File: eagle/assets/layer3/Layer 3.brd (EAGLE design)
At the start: 196 x 158 mm, 84 parts, among them Q2 AO3402, X1 SM06B-SRSS-TB, Y1 8MHz

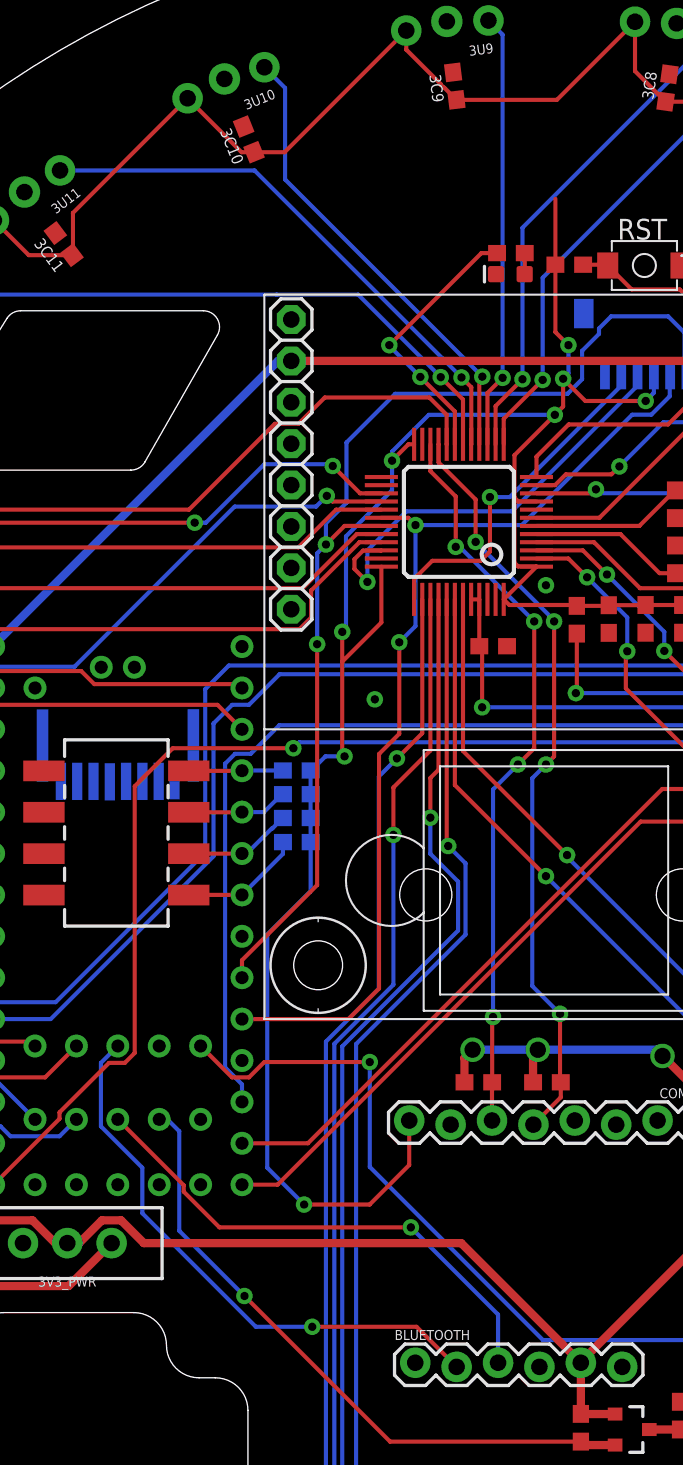
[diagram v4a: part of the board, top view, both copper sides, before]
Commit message: Edited teensy 4 pin out
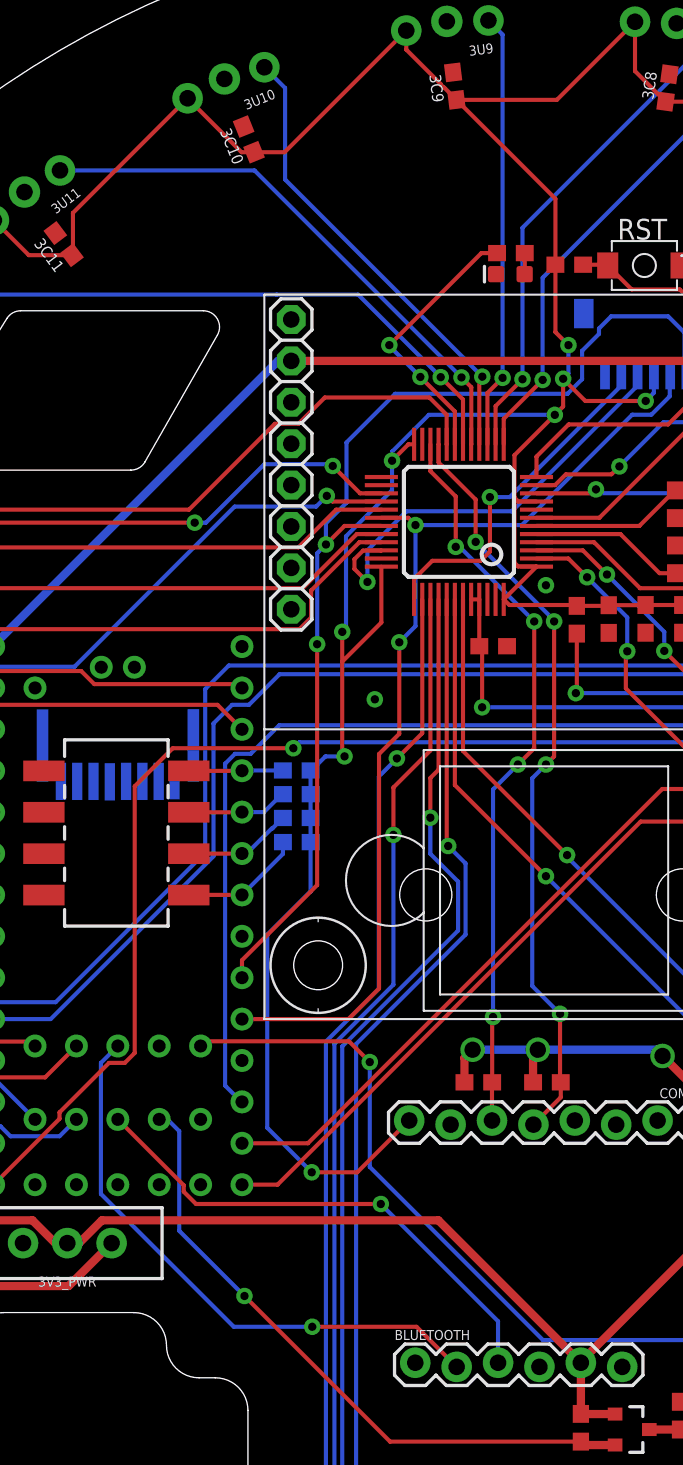
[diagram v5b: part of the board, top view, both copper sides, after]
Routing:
- net 3V3_SWITCH: track 577.5 -> 581.4 mm
- net RX_BT: track 34.9 -> 35.7 mm
- net ESC_LV: track 47.4 -> 46.9 mm
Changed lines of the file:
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@@
 </layers>
 <board>
-<fusionsync huburn="a.YnVzaW5lc3M6Z21haWwxNDMxNzc3" projecturn="a.YnVzaW5lc3M6Z21haWwxNDMxNzc3IzIwMjIwMTE1NDg1NTYyMzgx" f3durn="urn:adsk.wipprod:dm.lineage:7ikLfJsPR9eTqnN77vvEIg" pcbguid="" lastpulledtime="" lastsyncedchangeguid="" latestrevisionid="1eb35726-afcb-4420-9c79-5270dc816efc" lastsyncedrevisionid="1eb35726-afcb-4420-9c79-5270dc816efc" lastboardhashguid="961d5901-0f89-b416-3a91-9d1b3ab43cf4" lastpushedtime="2022-03-01T01:10:26Z" linktopcb3d="true"/>
+<fusionsync huburn="a.YnVzaW5lc3M6Z21haWwxNDMxNzc3" projecturn="a.YnVzaW5lc3M6Z21haWwxNDMxNzc3IzIwMjIwMTE1NDg1NTYyMzgx" f3durn="urn:adsk.wipprod:dm.lineage:7ikLfJsPR9eTqnN77vvEIg" pcbguid="" lastpulledtime="" lastsyncedchangeguid="" latestrevisionid="d040567a-c9aa-45d0-a0c7-126f738ef4e2" lastsyncedrevisionid="d040567a-c9aa-45d0-a0c7-126f738ef4e2" lastboardhashguid="c860b672-bc3c-8241-e7e5-cbe0f4989fd4" lastpushedtime="2022-03-01T08:50:26Z" linktopcb3d="true"/>
 <plain>
 <text x="-40.27" y="8.13" size="0.8128" layer="25" rot="R90">3.3V</text>
@@
 <wire x1="-35.8385875" y1="-19.9676125" x2="-42.802975" y2="-13.003225" width="0.508" layer="1"/>
 <wire x1="-32.0076" y1="-19.9676125" x2="-35.8385875" y2="-19.9676125" width="0.508" layer="1"/>
-<wire x1="-27.7453125" y1="-19.9676125" x2="-26.572" y2="-19.9676125" width="0.508" layer="1"/>
 <wire x1="-29.869209375" y1="-21.366409375" x2="-29.144109375" y2="-21.366409375" width="0.508" layer="1"/>
 <wire x1="-29.144109375" y1="-21.366409375" x2="-27.7453125" y2="-19.9676125" width="0.508" layer="1"/>
-<wire x1="-26.572" y1="-19.9676125" x2="-25.173203125" y2="-21.366409375" width="0.508" layer="1"/>
-<wire x1="-25.173203125" y1="-21.366409375" x2="-5.699090625" y2="-21.366409375" width="0.508" layer="1"/>
-<wire x1="-5.699090625" y1="-21.366409375" x2="1.64" y2="-28.7055" width="0.508" layer="1"/>
+<wire x1="-27.7453125" y1="-19.9676125" x2="-7.0978875" y2="-19.9676125" width="0.508" layer="1"/>
+<wire x1="-7.0978875" y1="-19.9676125" x2="1.64" y2="-28.7055" width="0.508" layer="1"/>
 <wire x1="3.743284375" y1="-31.8543625" x2="1.65240625" y2="-31.8543625" width="0.508" layer="1"/>
 <wire x1="1.65240625" y1="-31.8543625" x2="1.64371875" y2="-31.845675" width="0.508" layer="1"/>
@@
 <wire x1="45.571084375" y1="18.4119125" x2="45.571084375" y2="19.178815625" width="0.254" layer="1"/>
 <wire x1="45.571084375" y1="19.178815625" x2="48.880921875" y2="22.488653125" width="0.254" layer="1"/>
-<wire x1="0.079921875" y1="42.71384375" x2="0.079921875" y2="38.667053125" width="0.254" layer="1"/>
+<wire x1="0.079921875" y1="38.667053125" x2="0.079921875" y2="42.71384375" width="0.254" layer="1"/>
 <wire x1="-29.52406875" y1="41.84550625" x2="-29.52406875" y2="39.308071875" width="0.254" layer="1"/>
 <wire x1="-29.57920625" y1="39.252934375" x2="-29.52406875" y2="39.308071875" width="0.254" layer="1"/>
@@
 <wire x1="-1.097" y1="20.155" x2="-1.082" y2="20.14" width="0.254" layer="1"/>
 <wire x1="-2.43" y1="24.37548125" x2="-2.43" y2="20.37548125" width="0.254" layer="1"/>
-<wire x1="-15.34" y1="-19" x2="-11.3155" y2="-19" width="0.254" layer="1"/>
-<via x="-15.34" y="-19" extent="1-16" drill="0.508"/>
+<wire x1="-14.8705" y1="-17.0195" x2="-12.077" y2="-17.0195" width="0.254" layer="1"/>
+<via x="-14.8705" y="-17.0195" extent="1-16" drill="0.508"/>
 <wire x1="-17.6022" y1="-2.4444125" x2="-14.938325" y2="0.2194625" width="0.254" layer="16"/>
-<wire x1="-15.34" y1="-19" x2="-17.6022" y2="-16.7378" width="0.254" layer="16"/>
-<wire x1="-17.6022" y1="-16.7378" x2="-17.6022" y2="-2.4444125" width="0.254" layer="16"/>
+<wire x1="-14.8705" y1="-17.0195" x2="-17.6022" y2="-14.2878" width="0.254" layer="16"/>
+<wire x1="-17.6022" y1="-14.2878" x2="-17.6022" y2="-2.4444125" width="0.254" layer="16"/>
 <wire x1="-45.571084375" y1="-18.4119125" x2="-39.982996875" y2="-24" width="0.508" layer="1"/>
 <wire x1="-29.785" y1="-24" x2="-27.151409375" y2="-21.366409375" width="0.508" layer="1"/>
 <wire x1="-39.982996875" y1="-24" x2="-29.785" y2="-24" width="0.508" layer="1"/>
-<wire x1="-8.89" y1="-16.5745" x2="-8.89" y2="-13.843" width="0.254" layer="1"/>
-<wire x1="-11.3155" y1="-19" x2="-8.89" y2="-16.5745" width="0.254" layer="1"/>
-<wire x1="0.079921875" y1="42.71384375" x2="-5.989875" y2="48.783640625" width="0" layer="19" extent="1-1"/>
+<wire x1="-8.89" y1="-13.843" x2="-8.9005" y2="-13.843" width="0.254" layer="1"/>
+<wire x1="-8.9005" y1="-13.843" x2="-12.077" y2="-17.0195" width="0.254" layer="1"/>
+<wire x1="0.079921875" y1="42.71384375" x2="-5.989875" y2="48.783640625" width="0.254" layer="1"/>
 </signal>
 <signal name="5V_SWITCH">
@@
 <contactref element="TEENSY4" pad="D33"/>
 <via x="-11.31" y="-10.25683125" extent="1-16" drill="0.508"/>
-<wire x1="-17.78056875" y1="-10.25683125" x2="-11.31" y2="-10.25683125" width="0.254" layer="1"/>
-<wire x1="-18.7205375" y1="-11.1968" x2="-17.78056875" y2="-10.25683125" width="0.254" layer="1"/>
-<wire x1="-21.69" y1="-9.271" x2="-19.7642" y2="-11.1968" width="0.254" layer="1"/>
-<wire x1="-19.7642" y1="-11.1968" x2="-18.7205375" y2="-11.1968" width="0.254" layer="1"/>
+<wire x1="-12.586" y1="-8.98083125" x2="-21.39983125" y2="-8.98083125" width="0.254" layer="1"/>
+<wire x1="-21.69" y1="-9.271" x2="-21.39983125" y2="-8.98083125" width="0.254" layer="1"/>
+<wire x1="-12.586" y1="-8.98083125" x2="-11.31" y2="-10.25683125" width="0.254" layer="1"/>
 <wire x1="-11.31" y1="-10.25683125" x2="-11.31" y2="-16.69" width="0.254" layer="16"/>
 <wire x1="11.544853125" y1="-28.239759375" x2="13.310325" y2="-28.239759375" width="0.254" layer="16"/>
@@
 <wire x1="9.5198875" y1="10.4110875" x2="-16.8610875" y2="10.4110875" width="0.254" layer="16"/>
 <contactref element="TEENSY4" pad="D10"/>
-<wire x1="-19.15" y1="-12.7" x2="-19.15" y2="-11.6262625" width="0.254" layer="16"/>
-<wire x1="-19.15" y1="-11.6262625" x2="-20.1868" y2="-10.5894625" width="0.254" layer="16"/>
+<wire x1="-19.15" y1="-12.7" x2="-19.1867625" y2="-12.7" width="0.254" layer="16"/>
+<wire x1="-19.1867625" y1="-12.7" x2="-20.1868" y2="-11.6999625" width="0.254" layer="16"/>
 <wire x1="-20.1868" y1="8.0494625" x2="-19.5794625" y2="8.6568" width="0.254" layer="16"/>
 <wire x1="-18.615375" y1="8.6568" x2="-16.8610875" y2="10.4110875" width="0.254" layer="16"/>
 <wire x1="-19.5794625" y1="8.6568" x2="-18.615375" y2="8.6568" width="0.254" layer="16"/>
-<wire x1="-20.1868" y1="-10.5894625" x2="-20.1868" y2="8.0494625" width="0.254" layer="16"/>
+<wire x1="-20.1868" y1="-11.6999625" x2="-20.1868" y2="8.0494625" width="0.254" layer="16"/>
 </signal>
 <signal name="SDA0_TEE">
@@
 <contactref element="TEENSY4" pad="D29"/>
 <wire x1="-27.8068" y1="-10.3078" x2="-26.77" y2="-9.271" width="0.254" layer="16"/>
-<wire x1="-27.8068" y1="-10.3078" x2="-27.8068" y2="-14.2024625" width="0.254" layer="16"/>
-<wire x1="-25.2668" y1="-16.7424625" x2="-27.8068" y2="-14.2024625" width="0.254" layer="16"/>
-<wire x1="-25.2668" y1="-16.7424625" x2="-25.2668" y2="-19.53294375" width="0.254" layer="16"/>
-<wire x1="-18.29974375" y1="-26.5" x2="-14.84" y2="-26.5" width="0.254" layer="16"/>
+<wire x1="-27.8068" y1="-10.3078" x2="-27.8068" y2="-18.34844375" width="0.254" layer="16"/>
+<wire x1="-19.65524375" y1="-26.5" x2="-14.84" y2="-26.5" width="0.254" layer="16"/>
 <via x="-14.84" y="-26.5" extent="1-16" drill="0.508"/>
 <wire x1="-14.84" y1="-26.5" x2="-8.4395" y2="-26.5" width="0.254" layer="1"/>
 <wire x1="-8.4395" y1="-26.5" x2="-5.98" y2="-28.9595" width="0.254" layer="1"/>
-<wire x1="-25.2668" y1="-19.53294375" x2="-18.29974375" y2="-26.5" width="0.254" layer="16"/>
+<wire x1="-27.8068" y1="-18.34844375" x2="-19.65524375" y2="-26.5" width="0.254" layer="16"/>
 </signal>
 <signal name="TX_BT">
@@
 <wire x1="-26.77" y1="-13.773" x2="-22.7268" y2="-17.8162" width="0.254" layer="1"/>
 <wire x1="-22.7268" y1="-17.8162" x2="-22.7268" y2="-18.2094625" width="0.254" layer="1"/>
-<wire x1="-20.53685625" y1="-20.39940625" x2="-8.7885375" y2="-20.39940625" width="0.254" layer="1"/>
-<via x="-8.7885375" y="-20.39940625" extent="1-16" drill="0.508"/>
-<wire x1="-8.7885375" y1="-20.39940625" x2="-3.44" y2="-25.74794375" width="0.254" layer="16"/>
-<wire x1="-3.44" y1="-25.74794375" x2="-3.44" y2="-28.7055" width="0.254" layer="16"/>
-<wire x1="-22.7268" y1="-18.2094625" x2="-20.53685625" y2="-20.39940625" width="0.254" layer="1"/>
+<wire x1="-21.96985625" y1="-18.96640625" x2="-10.6340375" y2="-18.96640625" width="0.254" layer="1"/>
+<via x="-10.6340375" y="-18.96640625" extent="1-16" drill="0.508"/>
+<wire x1="-10.6340375" y1="-18.96640625" x2="-3.44" y2="-26.16044375" width="0.254" layer="16"/>
+<wire x1="-3.44" y1="-26.16044375" x2="-3.44" y2="-28.7055" width="0.254" layer="16"/>
+<wire x1="-22.7268" y1="-18.2094625" x2="-21.96985625" y2="-18.96640625" width="0.254" layer="1"/>
 </signal>
 <signal name="SERVO_HV">

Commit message: Edited cura
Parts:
- removed COMPASS: BNO055, JH:BNO055
- added BNO055: (no value), SparkFun-Connectors:1X08_LOCK
- moved R10 28.0 mm to (-3.65, -39.5), flipped to the bottom
- moved R11 28.0 mm to (0.44, -39.5), flipped to the bottom, turned to 0 degrees
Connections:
- net 3V3_SWITCH: now also BNO055.8; no longer COMPASS.8
- net GND: now also BNO055.7; no longer COMPASS.7
- net SCL1: now also BNO055.5; no longer COMPASS.5
- net SDA1: now also BNO055.6; no longer COMPASS.6
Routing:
- net SDA1: track 45.3 -> 102.4 mm, vias 4 -> 7
- net SCL1: track 46.7 -> 98.0 mm, vias 4 -> 7
- net 3.3V: track 122.0 -> 96.0 mm, vias 3 -> 0
- net 3V3_SWITCH: track 581.4 -> 559.5 mm, vias 9 -> 8
- net ESC_LV: track 46.9 -> 43.2 mm
- net TX_BT: track 31.2 -> 32.8 mm
- net IR1: track 78.6 -> 77.6 mm
